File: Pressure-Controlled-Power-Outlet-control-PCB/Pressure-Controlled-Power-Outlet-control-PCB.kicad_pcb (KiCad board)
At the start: 4 copper layers, 100.3 x 86.4 mm, 31 parts, among them J1 Analog water pressure sensor 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, J2 1017514, J3 I2C0 Connector, J4 SPI1 Connector, K1 T9GV5L24-24, K2 T9GV5L24-24, Q1 2N3906, Q2 IRF540N, Q3 IRF540N, Q4 2N3906, U1 Pico, U2 LM324, U3 LF50_TO220

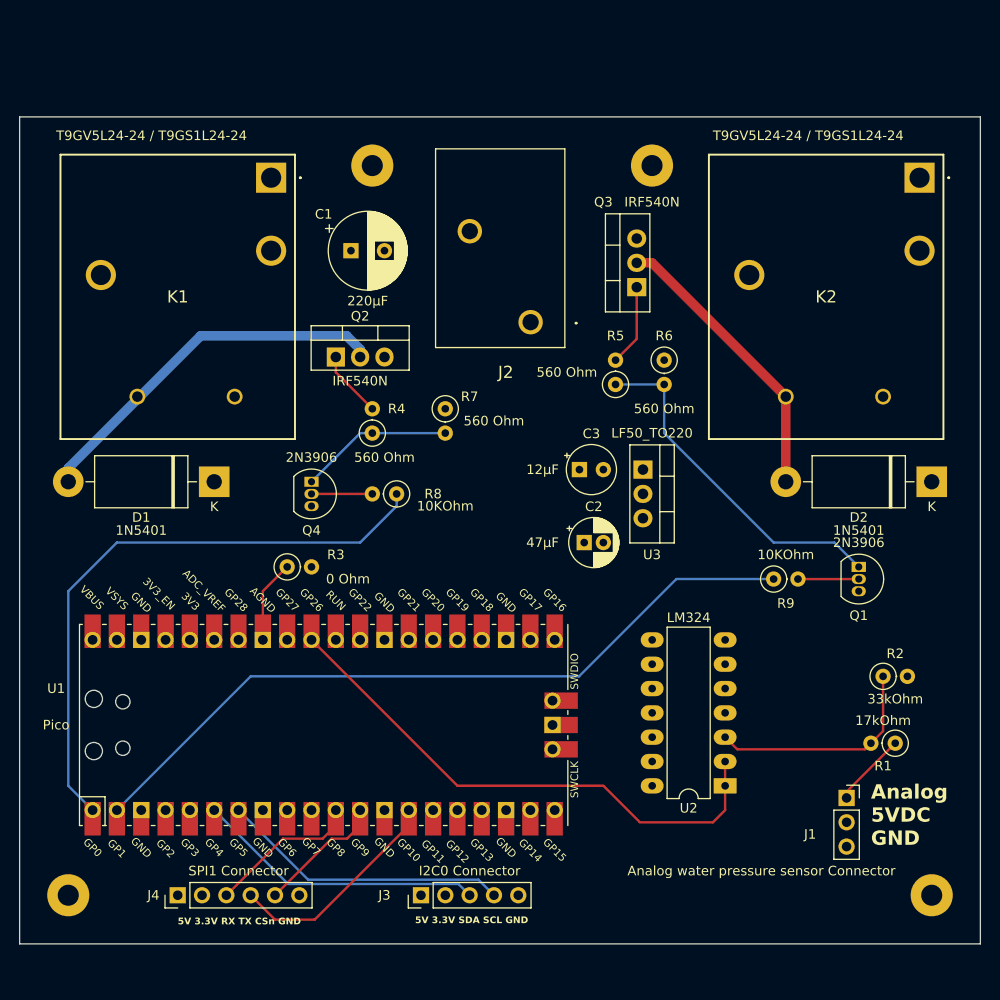
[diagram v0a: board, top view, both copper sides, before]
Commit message: sign a new feature creep added two fan headers that can power ether 24 or 5 volt fans
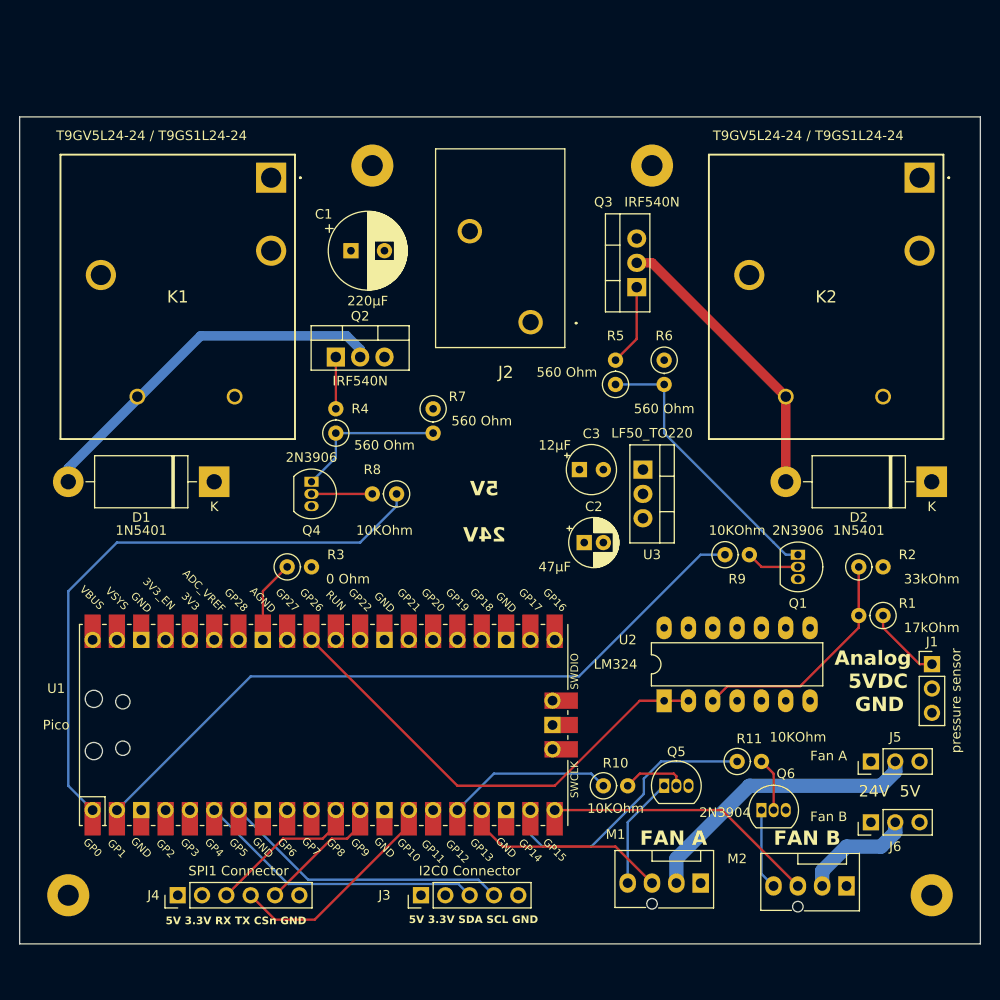
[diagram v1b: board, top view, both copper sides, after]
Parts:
- added J5: FanA 5V/24V, Connector_PinHeader_2.54mm:PinHeader_1x03_P2.54mm_Vertical, F.Cu at (175.3, 133.3)
- added J6: FanB 5V/24V, Connector_PinHeader_2.54mm:PinHeader_1x03_P2.54mm_Vertical, F.Cu at (175.3, 139.7)
- added M1: Fan_4pin, Connector:FanPinHeader_1x04_P2.54mm_Vertical, F.Cu at (157.5, 146.1)
- added M2: Fan_4pin, Connector:FanPinHeader_1x04_P2.54mm_Vertical, F.Cu at (172.7, 146.3)
- added Q5: 2N3904, Package_TO_SOT_THT:TO-92_Inline, F.Cu at (153.7, 135.9)
- added Q6: 2N3904, Package_TO_SOT_THT:TO-92_Inline, F.Cu at (163.8, 138.4)
- added R10: 10KOhm, Resistor_THT:R_Axial_DIN0207_L6.3mm_D2.5mm_P2.54mm_Vertical, F.Cu at (147.3, 135.9)
- added R11: 10KOhm, Resistor_THT:R_Axial_DIN0207_L6.3mm_D2.5mm_P2.54mm_Vertical, F.Cu at (161.3, 133.3)
- J1: value Analog water pressure sensor Connector -> pressure sensor; footprint Connector_PinSocket_2.54mm:PinSocket_1x03_P2.54mm_Vertical -> Connector_PinHeader_2.54mm:PinHeader_1x03_P2.54mm_Vertical
- moved J1 16.6 mm to (181.6, 123.2)
- moved R1 13.4 mm to (176.5, 118.1)
- moved R2 11.7 mm to (174.0, 113.0)
- moved U2 10.9 mm to (153.7, 127.0), turned to 90 degrees
- moved Q1 6.48 mm to (167.6, 111.8)
- moved R9 5.68 mm to (160.0, 111.8)
- moved R4 3.81 mm to (119.4, 99.1)
- moved R7 1.27 mm to (129.5, 96.5)
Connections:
- U1 pad 16: unconnected-(U1-GPIO12-Pad16) -> /FanA_PWM
- U1 pad 17: unconnected-(U1-GPIO13-Pad17) -> /FanA_Tac
- U1 pad 19: unconnected-(U1-GPIO14-Pad19) -> /FanB_PWM
- U1 pad 20: unconnected-(U1-GPIO15-Pad20) -> /FanB_Tac
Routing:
- net +24V: track 0.00 -> 38.2 mm
- net /FanA_Power: track 0.00 -> 30.2 mm
- net /FanB_PWM: track 0.00 -> 29.3 mm
- net /FanB_Tac: track 0.00 -> 28.7 mm
- net /FanA_Tac: track 0.00 -> 21.9 mm
- net /FanA_PWM: track 0.00 -> 17.3 mm
- net /FanB_Power: track 0.00 -> 11.9 mm
- net Net-(M1-PWM): track 0.00 -> 11.7 mm
- net Net-(M2-PWM): track 0.00 -> 8.44 mm
- net /ADC0: track 56.7 -> 49.4 mm
- net Net-(Q1-E): track 36.3 -> 29.4 mm
- net Net-(Q5-B): track 0.00 -> 6.72 mm
- net Net-(Q6-B): track 0.00 -> 5.76 mm
- net /Activate_Neutral: track 78.6 -> 74.5 mm
- net Net-(Q2-G): track 6.98 -> 5.41 mm
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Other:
- board text added: "24V 5V"
- board text added: "5V 24V"
- board text added: "FAN A"
- board text added: "FAN B"
- board text added: "Fan A"
- board text added: "Fan B"

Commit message: hopefully final push for the day
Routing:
- net /ADC0: track 49.4 -> 42.0 mm
- net /Water Pressure 5V: track 7.95 -> 7.23 mm
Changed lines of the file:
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@@
   (segment (start 149.86 146.05) (end 149.86 139.7) (width 0.25) (layer "B.Cu") (net 13))
   (segment (start 149.86 139.7) (end 153.67 135.89) (width 0.25) (layer "B.Cu") (net 13))
-  (segment (start 142.24 135.89) (end 132.08 135.89) (width 0.25) (layer "F.Cu") (net 22))
-  (segment (start 132.08 135.89) (end 116.84 120.65) (width 0.25) (layer "F.Cu") (net 22))
-  (segment (start 151.115 127.015) (end 142.24 135.89) (width 0.25) (layer "F.Cu") (net 22))
+  (segment (start 148.56 124.46) (end 120.65 124.46) (width 0.25) (layer "F.Cu") (net 22))
+  (segment (start 151.115 127.015) (end 148.56 124.46) (width 0.25) (layer "F.Cu") (net 22))
   (segment (start 156.205 127.015) (end 151.115 127.015) (width 0.25) (layer "F.Cu") (net 22))
+  (segment (start 120.65 124.46) (end 116.84 120.65) (width 0.25) (layer "F.Cu") (net 22))
   (segment (start 111.76 120.65) (end 111.76 115.57) (width 0.25) (layer "F.Cu") (net 24))
   (segment (start 111.76 115.57) (end 114.3 113.03) (width 0.25) (layer "F.Cu") (net 24))
@@
   (segment (start 118.945 141.405) (end 120.555 141.405) (width 0.25) (layer "F.Cu") (net 26))
   (segment (start 121.92 140.04) (end 121.92 138.43) (width 0.25) (layer "F.Cu") (net 26))
-  (segment (start 176.53 119.38) (end 176.53 118.11) (width 0.25) (layer "F.Cu") (net 32))
-  (segment (start 181.635 123.19) (end 180.34 123.19) (width 0.25) (layer "F.Cu") (net 32))
-  (segment (start 180.34 123.19) (end 176.53 119.38) (width 0.25) (layer "F.Cu") (net 32))
+  (segment (start 181.61 123.19) (end 176.53 118.11) (width 0.25) (layer "F.Cu") (net 32))
+  (segment (start 181.635 123.19) (end 181.61 123.19) (width 0.25) (layer "F.Cu") (net 32))
+  (segment (start 181.635 123.19) (end 181.61 123.19) (width 0.25) (layer "B.Cu") (net 32))
   (segment (start 167.88 125.49) (end 173.99 119.38) (width 0.25) (layer "F.Cu") (net 33))
   (segment (start 158.745 127.015) (end 160.27 125.49) (width 0.25) (layer "F.Cu") (net 33))

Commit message: hopefully final rev for the night
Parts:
- moved Q1 9.16 mm to (160.0, 106.7)
- moved C3 8.93 mm to (135.9, 102.9)
- moved C2 8.89 mm to (136.4, 110.5)
- moved R9 8.52 mm to (152.4, 108.0)
- moved U3 7.62 mm to (143.8, 102.9)
- moved Q6 7.41 mm to (167.6, 132.1)
- moved J1 6.47 mm to (182.9, 116.8)
- moved U2 5.68 mm to (151.1, 121.9)
- moved R1 5.39 mm to (172.7, 114.3)
- moved R2 4.58 mm to (170.2, 110.5)
- moved R11 4.58 mm to (158.8, 129.5)
- moved Q5 1.27 mm to (153.7, 134.6)
- moved R10 1.27 mm to (147.3, 134.6)
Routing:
- net Net-(Q1-E): track 29.4 -> 20.4 mm
- net Net-(M2-PWM): track 8.44 -> 15.3 mm
- net /Water Pressure 5V: track 7.23 -> 11.2 mm
- net Net-(U2A-+): track 24.8 -> 28.2 mm
- net Net-(Q6-B): track 5.76 -> 9.06 mm
- net /Activate_Neutral: track 74.5 -> 71.9 mm
- net /ADC0: track 42.0 -> 39.4 mm
- net Net-(M1-PWM): track 11.7 -> 13.0 mm
- net /FanB_PWM: track 29.3 -> 28.5 mm
- net /FanA_PWM: track 17.3 -> 16.8 mm
- net Net-(Q1-B): track 5.61 -> 5.08 mm
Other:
- board text removed: "5V 24V"

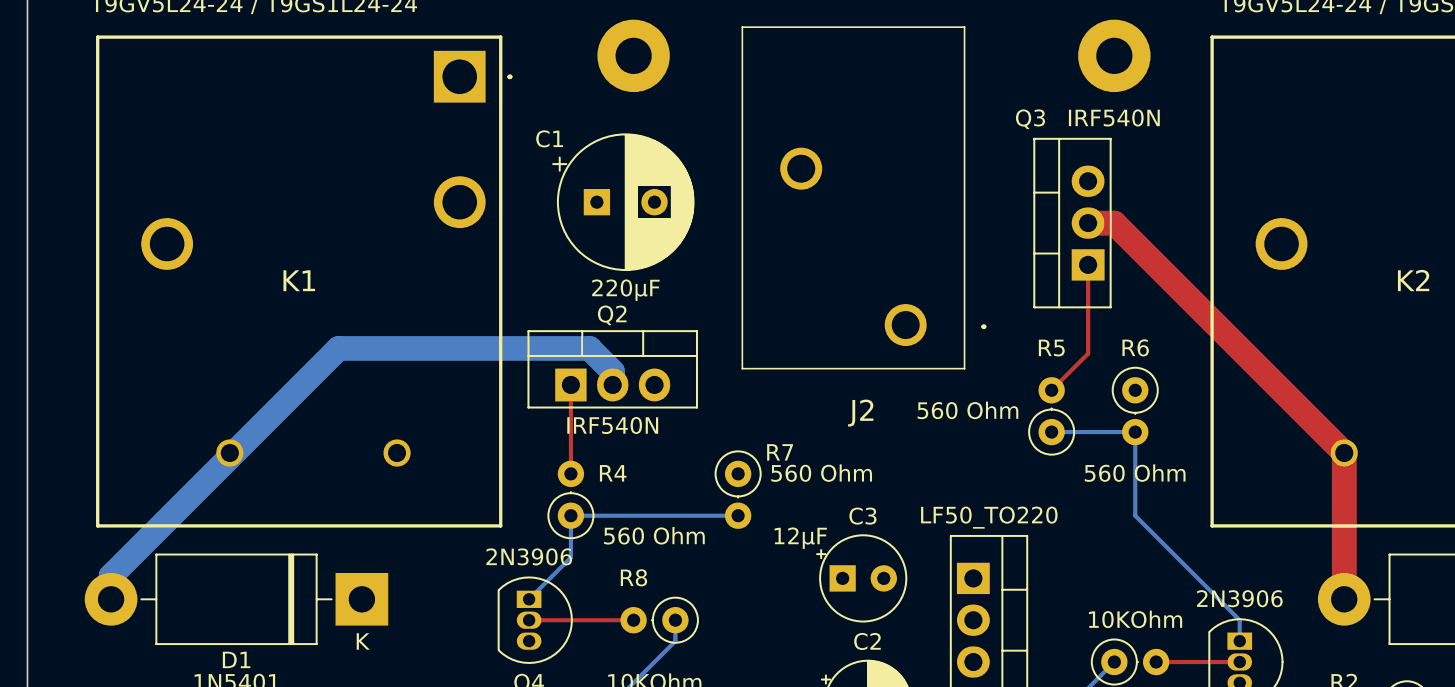
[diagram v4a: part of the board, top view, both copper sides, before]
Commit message: added name to pcb
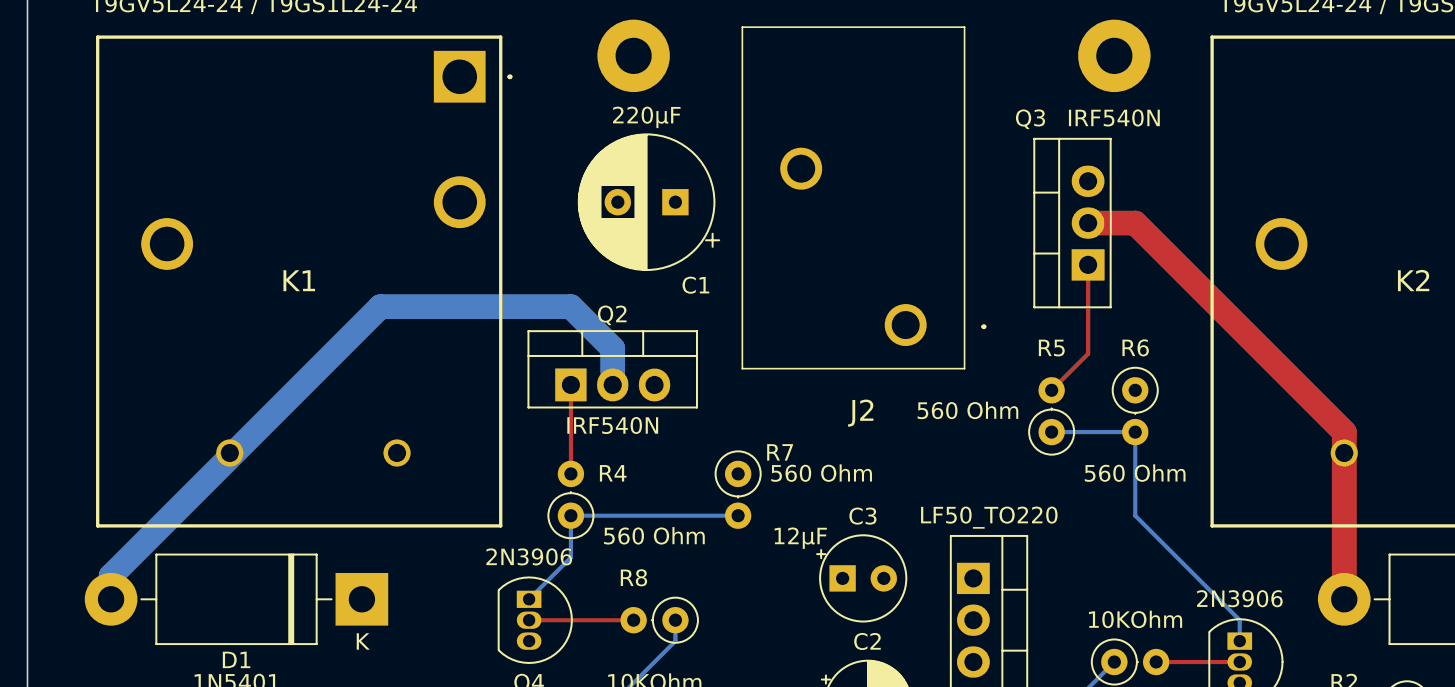
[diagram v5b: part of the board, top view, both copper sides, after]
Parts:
- moved C1 4.77 mm to (125.7, 80.0), turned to 180 degrees
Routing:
- net Net-(D1-A): track 39.0 -> 41.9 mm
- net Net-(D2-A): track 30.2 -> 31.0 mm
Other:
- board text added: "Pressure Controlled Power Outlet control PCB 2024-07-19 V1.2.3 By Brian Banas"
- board text removed: "Pressure Controlled Power Outlet control PCB 2024-07-19 V1.1.1"
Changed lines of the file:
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@@
     (title "Pressure Controlled Power Outlet")
     (date "2024-07-18")
-    (rev "V1.2.2")
-    (company "Brian")
+    (rev "V1.2.3")
+    (company "Brian Banas")
   )
   (layers
@@
   )
   (footprint "Capacitor_THT:CP_Radial_D8.0mm_P3.50mm" (layer "F.Cu")
-    (at 120.96 80.01)
+    (at 125.73 80.01 180)
     (descr "CP, Radial series, Radial, pin pitch=3.50mm, , diameter=8mm, Electrolytic Capacitor")
     (tags "CP Radial series Radial pin pitch 3.50mm  diameter 8mm Electrolytic Capacitor")
@@
     (property "ki_keywords" "cap capacitor")
     (attr through_hole)
-    (fp_text reference "C1" (at -2.85 -3.81) (layer "F.SilkS")
+    (fp_text reference "C1" (at -1.27 -5.08) (layer "F.SilkS")
         (effects (font (size 1 1) (thickness 0.15)))
     )
@@
     (fp_circle (center 1.75 0) (end 5.75 0)
       (stroke (width 0.1) (type solid)) (fill none) (layer "F.Fab"))
-    (pad "1" thru_hole rect (at 0 0) (size 1.6 1.6) (drill 0.8) (layers "*.Cu" "*.Mask")
+    (pad "1" thru_hole rect (at 0 0 180) (size 1.6 1.6) (drill 0.8) (layers "*.Cu" "*.Mask")
       (net 34 "+24V") (pintype "passive"))
-    (pad "2" thru_hole circle (at 3.5 0) (size 1.6 1.6) (drill 0.8) (layers "*.Cu" "*.Mask")
+    (pad "2" thru_hole circle (at 3.5 0 180) (size 1.6 1.6) (drill 0.8) (layers "*.Cu" "*.Mask")
       (net 1 "GND") (pintype "passive"))
     (model "${KICAD6_3DMODEL_DIR}/Capacitor_THT.3dshapes/CP_Radial_D8.0mm_P3.50mm.wrl"
@@
   (gr_rect (start 86.36 66.04) (end 186.69 152.4)
     (stroke (width 0.1) (type default)) (fill none) (layer "Edge.Cuts"))
-  (gr_text "Pressure Controlled Power Outlet control PCB\n2024-07-19\nV1.1.1\n" (at 90.17 107.95 180) (layer "B.SilkS")
+  (gr_text "Pressure Controlled Power Outlet control PCB\n2024-07-19\nV1.2.3\nBy Brian Banas" (at 90.17 107.95 180) (layer "B.SilkS")
     (effects (font (size 2 2) (thickness 0.15)) (justify left bottom mirror))
   )
@@
   (segment (start 175.26 133.35) (end 175.26 120.65) (width 2.5) (layer "In1.Cu") (net 34))
   (segment (start 121.92 91.115) (end 121.92 90.3025) (width 1) (layer "B.Cu") (net 35))
+  (segment (start 107.805 86.36) (end 91.44 102.725) (width 1.5) (layer "B.Cu") (net 35))
+  (segment (start 119.38 86.36) (end 107.805 86.36) (width 1.5) (layer "B.Cu") (net 35))
   (segment (start 91.44 102.725) (end 91.44 104.14) (width 1.5) (layer "B.Cu") (net 35))
-  (segment (start 120.5175 88.9) (end 105.265 88.9) (width 1.5) (layer "B.Cu") (net 35))
-  (segment (start 105.265 88.9) (end 91.44 102.725) (width 1.5) (layer "B.Cu") (net 35))
-  (segment (start 121.92 90.3025) (end 120.5175 88.9) (width 1.5) (layer "B.Cu") (net 35))
-  (segment (start 150.805 81.28) (end 152.4 81.28) (width 1.5) (layer "F.Cu") (net 36))
-  (segment (start 152.4 81.28) (end 166.37 95.25) (width 1.5) (layer "F.Cu") (net 36))
+  (segment (start 121.92 90.3025) (end 121.92 88.9) (width 1.5) (layer "B.Cu") (net 35))
+  (segment (start 121.92 88.9) (end 119.38 86.36) (width 1.5) (layer "B.Cu") (net 35))
+  (segment (start 166.37 93.98) (end 166.37 95.25) (width 1.5) (layer "F.Cu") (net 36))
   (segment (start 166.37 95.25) (end 166.37 104.14) (width 1.5) (layer "F.Cu") (net 36))
+  (segment (start 153.67 81.28) (end 166.37 93.98) (width 1.5) (layer "F.Cu") (net 36))
+  (segment (start 150.805 81.28) (end 153.67 81.28) (width 1.5) (layer "F.Cu") (net 36))
   (segment (start 160.02 106.68) (end 160.02 105.41) (width 0.25) (layer "B.Cu") (net 37))
   (segment (start 153.67 99.06) (end 153.67 93.98) (width 0.25) (layer "B.Cu") (net 37))

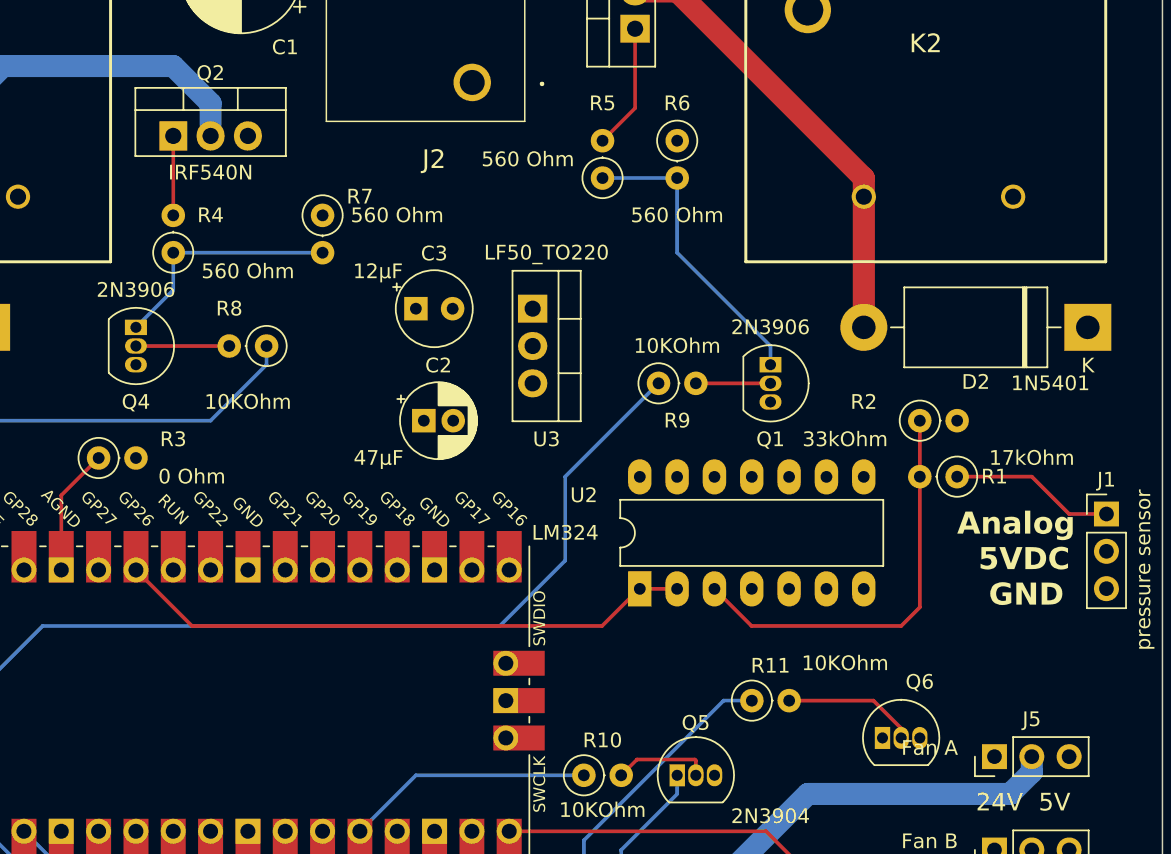
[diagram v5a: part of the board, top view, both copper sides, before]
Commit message: done for the day fixed some part spacing and traces
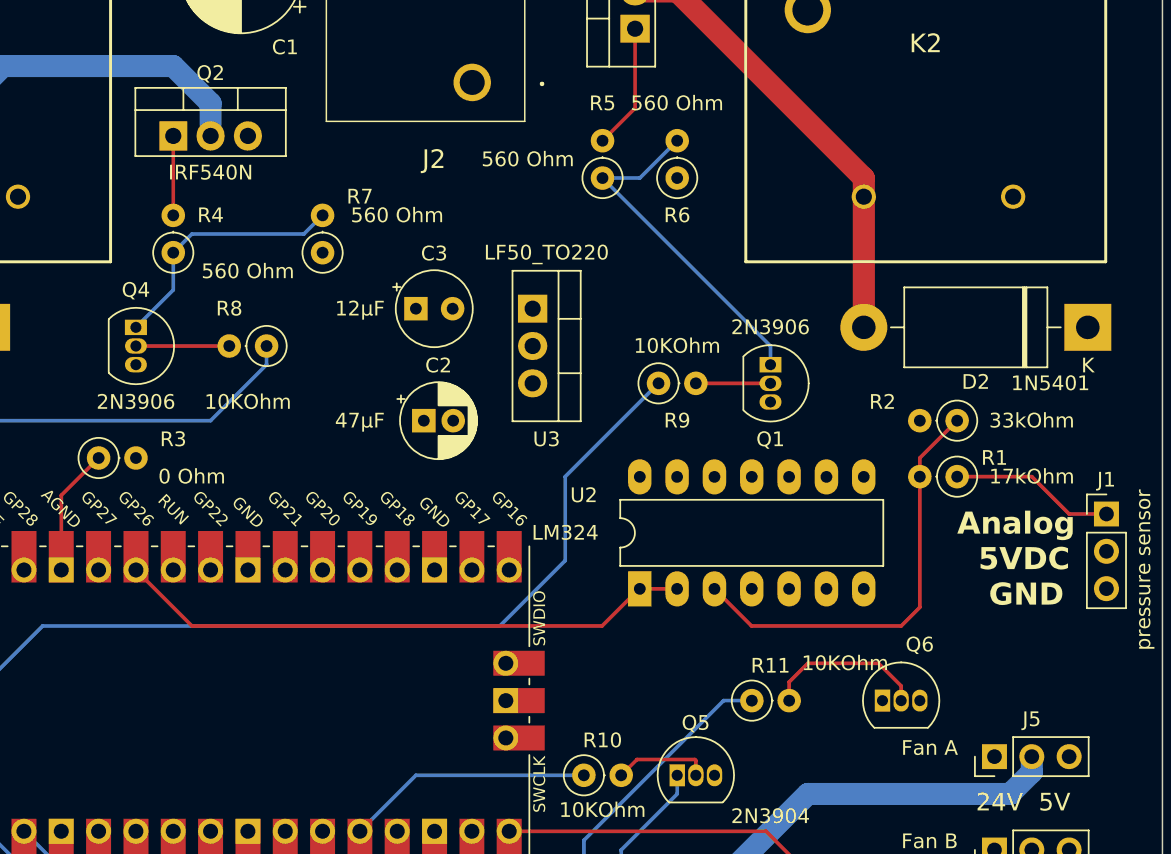
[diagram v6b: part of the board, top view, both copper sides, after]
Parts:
- moved Q6 2.54 mm to (167.6, 129.5)
- moved R6 2.54 mm to (153.7, 94.0), turned to 90 degrees
- moved R7 2.54 mm to (129.5, 99.1), turned to 90 degrees
- moved R2 2.54 mm to (172.7, 110.5), turned to 180 degrees
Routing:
- net Net-(Q1-E): track 20.4 -> 23.6 mm
- net Net-(M2-PWM): track 15.3 -> 17.9 mm
- net Net-(Q6-B): track 9.06 -> 11.1 mm
- net Net-(Q4-E): track 16.3 -> 17.3 mm
- net Net-(U2A-+): track 28.2 -> 29.3 mm
